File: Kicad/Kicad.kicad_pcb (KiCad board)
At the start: 4 copper layers, 6 parts, among them J1 USB_C_Receptacle_USB2.0, U1 MIMXRT685SFVKB, X1 ECS-2520MV-xxx-xx

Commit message: power section
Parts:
- D1: moved to F.Cu
- J1: footprint Connector_USB:USB_C_Receptacle_Amphenol_12401548E4-2A -> Connector_USB:USB_C_Receptacle_HRO_TYPE-C-31-M-12; moved to F.Cu
- moved X1 33.8 mm to (95.2, 66.3), turned to 0 degrees
- moved J1 12.4 mm to (76.5, 77.7), turned to -90 degrees
- moved L1 12.1 mm to (86.0, 82.0)
- moved U1 10.9 mm to (97.5, 74.5), turned to 180 degrees
- moved D1 10.4 mm to (86.2, 77.8), turned to -90 degrees
- moved C1 8.39 mm to (86.5, 85.0)
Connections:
- U1 pad A13: (no net) -> +1V8
- U1 pad B11: VDD1V8 -> +1V8
- U1 pad B16: (no net) -> /DSP/MODE1
- U1 pad C13: VDD_AO1V8 -> +1V8
- U1 pad C16: VDD1V8 -> +1V8
- U1 pad C17: VDD1V8 -> +1V8
- U1 pad D13: VDD_AO1V8 -> +1V8
- U1 pad E10: VDDIO_1 -> +3V3
- U1 pad E15: VDD1V8 -> +1V8
- U1 pad E4: unconnected-(U1-PadE4) -> +1V8
- U1 pad E6: VDDIO_1 -> +3V3
- U1 pad E8: VDDIO_1 -> +3V3
- U1 pad F13: VDD1V8 -> +1V8
- U1 pad F5: VDDIO_0 -> +3V3
- U1 pad G14: VDD1V8 -> +1V8
- U1 pad H13: VDDIO_1 -> +3V3
- U1 pad H14: VDDIO_1 -> +3V3
- U1 pad H5: VDDIO_0 -> +3V3
- U1 pad K13: VDDIO_1 -> +3V3
- U1 pad K5: VDDIO_0 -> +3V3
- U1 pad L14: VDDIO_1 -> +3V3
- U1 pad L4: VDD1V8 -> +1V8
- U1 pad M5: VDDIO_0 -> +3V3
- U1 pad N10: VDDIO_0 -> +3V3
- U1 pad N12: VDDIO_2 -> +3V3
- U1 pad N6: VDDIO_0 -> +3V3
- U1 pad N8: VDDIO_0 -> +3V3
- U1 pad P11: VDDIO_2 -> +3V3
- U1 pad P12: VDDIO_2 -> +3V3
- U1 pad R15: VDD1V8 -> +1V8
- U1 pad R17: /DSP/USB1_DP -> /USB/D+
- U1 pad T17: /DSP/USB1_DM -> /USB/D-
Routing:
- net GND: track 2.06 -> 0.00 mm, vias 3 -> 0
- net /DSP/XTALOUT: track 1.31 -> 0.00 mm
- net VDDIO_1: track 1.00 -> 0.00 mm, vias 2 -> 0
- net VDDIO_0: track 1.00 -> 0.00 mm, vias 2 -> 0
- net VDDIO_2: track 0.50 -> 0.00 mm, vias 1 -> 0
- net VDDCORE: track 0.50 -> 0.00 mm, vias 1 -> 0
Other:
- copper layers 4 -> 2

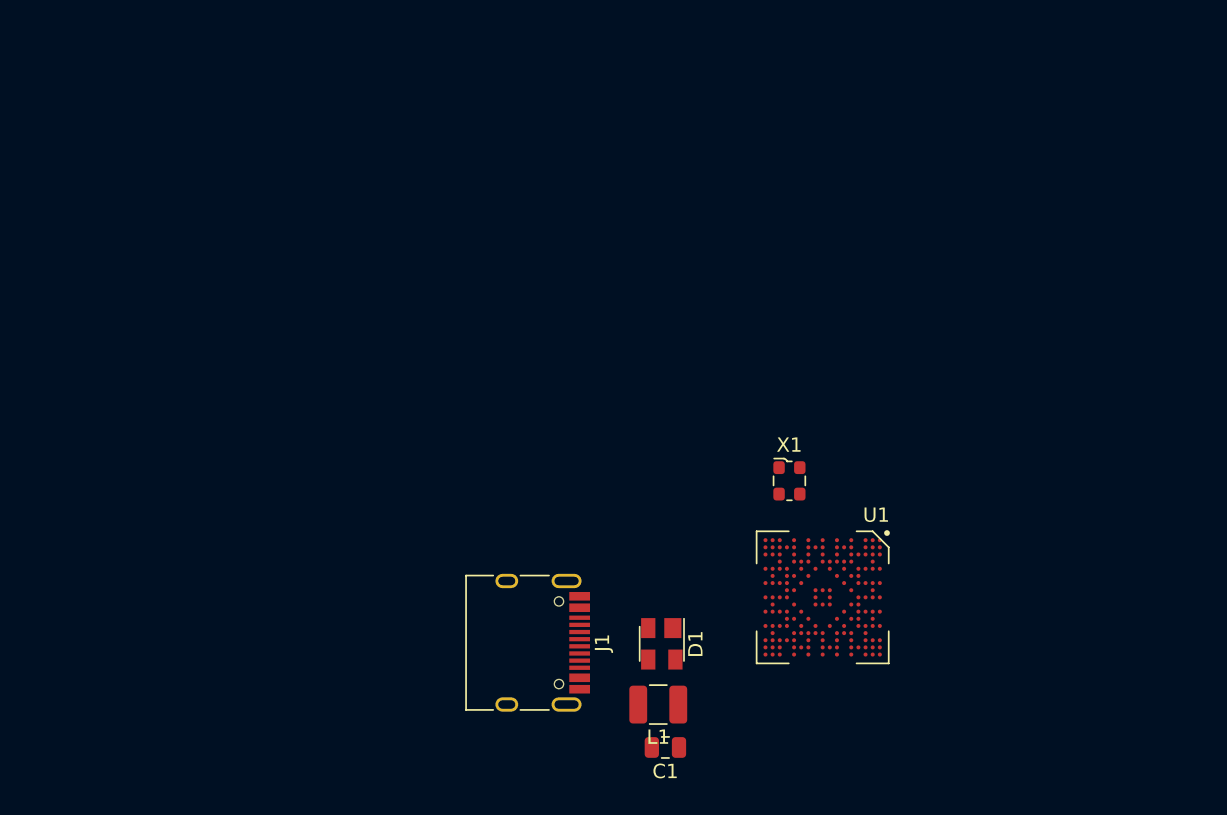
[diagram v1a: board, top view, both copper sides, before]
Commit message: Basic Power layout done
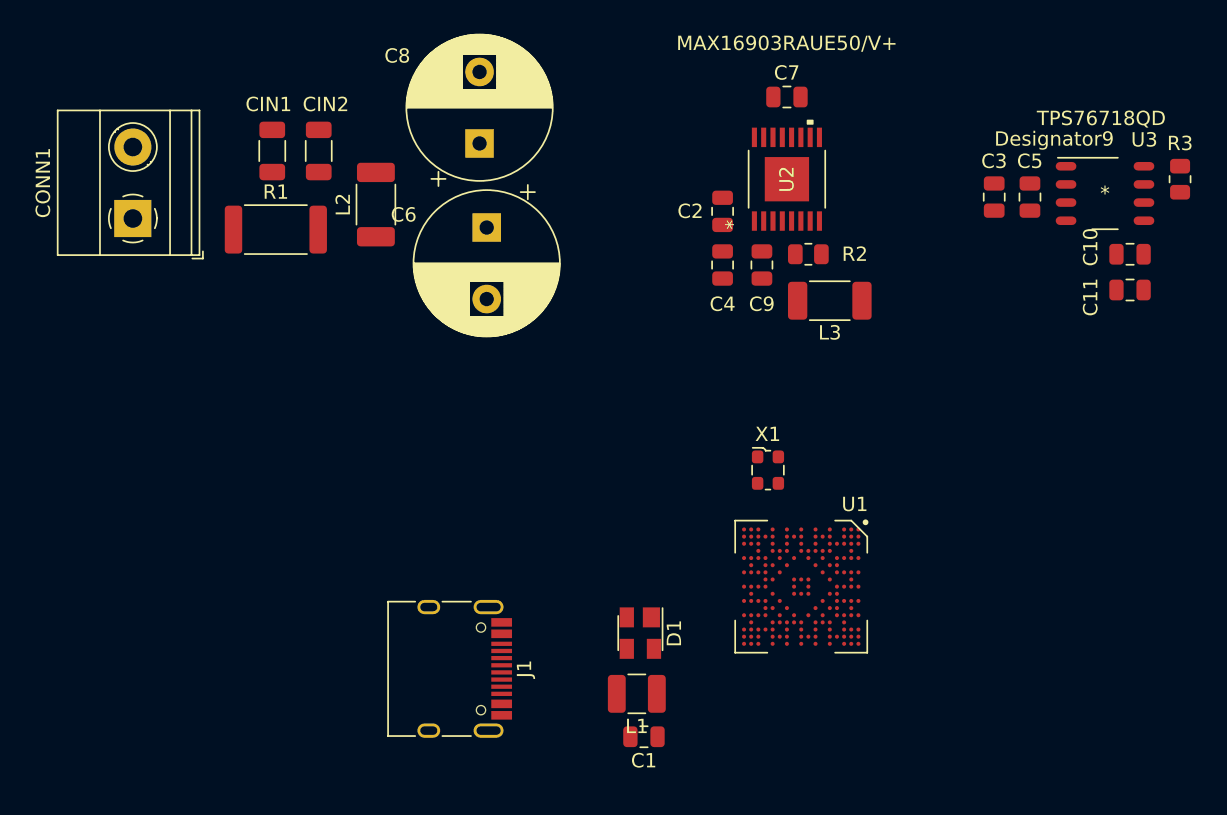
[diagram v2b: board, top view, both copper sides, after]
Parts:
- added C10: 10uF, Capacitor_SMD:C_0805_2012Metric, F.Cu at (119.0, 50.5)
- added C11: 10uF, Capacitor_SMD:C_0805_2012Metric, F.Cu at (119.0, 53.0)
- added C2: 4u7, Capacitor_SMD:C_0805_2012Metric, F.Cu at (90.5, 47.5)
- added C3: 1u, Capacitor_SMD:C_0805_2012Metric, F.Cu at (109.5, 46.5)
- added C4: 4u7, Capacitor_SMD:C_0805_2012Metric, F.Cu at (90.5, 51.2)
- added C5: 1u, Capacitor_SMD:C_0805_2012Metric, F.Cu at (112.0, 46.5)
- added C6: 100uF, Capacitor_THT:CP_Radial_D10.0mm_P5.00mm, F.Cu at (74.0, 48.6)
- added C7: 1u, Capacitor_SMD:C_0805_2012Metric, F.Cu at (95.0, 39.5)
- added C8: 100uF, Capacitor_THT:CP_Radial_D10.0mm_P5.00mm, F.Cu at (73.5, 42.8)
- added C9: 1u, Capacitor_SMD:C_0805_2012Metric, F.Cu at (93.2, 51.2)
- added CIN1: 0.022uF, Capacitor_SMD:C_1206_3216Metric, F.Cu at (59.0, 43.3)
- added CIN2: 0.022uF, Capacitor_SMD:C_1206_3216Metric, F.Cu at (62.2, 43.3)
- added CONN1: Screw_Terminal_01x02, TerminalBlock_Phoenix:TerminalBlock_Phoenix_MKDS-1,5-2_1x02_P5.00mm_Horizontal, F.Cu at (49.2, 48.0)
- added L2: 47, Inductor_SMD:L_2010_5025Metric, F.Cu at (66.2, 47.0)
- added L3: 4u7, Inductor_SMD:L_2010_5025Metric, F.Cu at (98.0, 53.8)
- added R1: 0.1R, Resistor_SMD:R_2512_6332Metric, F.Cu at (59.2, 48.8)
- added R2: 20k, Resistor_SMD:R_0805_2012Metric, F.Cu at (96.5, 50.5)
- added R3: 10k, Resistor_SMD:R_0805_2012Metric, F.Cu at (122.5, 45.2)
- added U2: MAX16903RAUE50/V+, project_footprints:MAX16903RAUE50&slash_V&plus_, F.Cu at (95.0, 45.2)
- added U3: TPS76718QD, project_footprints:TPS76718QD, F.Cu at (117.2, 46.2)
- moved J1 5.75 mm to (71.0, 79.5)
- moved C1 1.68 mm to (85.0, 84.2)
- moved D1 1.68 mm to (84.8, 77.0)
- moved L1 1.68 mm to (84.5, 81.2)
- moved U1 1.68 mm to (96.0, 73.8)
- moved X1 1.68 mm to (93.7, 65.6)

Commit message: working on DSP
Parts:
- added C12: 0.1u, Capacitor_SMD:C_0805_2012Metric, F.Cu at (141.8, 101.7)
- added C13: 1u, Capacitor_SMD:C_0805_2012Metric, F.Cu at (152.0, 95.2)
- added C14: 10u, Capacitor_SMD:C_0805_2012Metric, F.Cu at (154.2, 98.2)
- added C15: 0.1u, Capacitor_SMD:C_0805_2012Metric, F.Cu at (147.8, 104.2)
- added C16: 2.2u, Capacitor_SMD:C_0805_2012Metric, F.Cu at (153.0, 103.0)
- added C17: 0.1u, Capacitor_SMD:C_0805_2012Metric, F.Cu at (152.0, 98.2)
- added C18: 0.1u, Capacitor_SMD:C_0805_2012Metric, F.Cu at (140.2, 104.2)
- added C19: 0.1u, Capacitor_SMD:C_0805_2012Metric, F.Cu at (144.2, 104.2)
- added C20: 2.2u, Capacitor_SMD:C_0805_2012Metric, F.Cu at (147.8, 106.5)
- added C21: 10u, Capacitor_SMD:C_0805_2012Metric, F.Cu at (144.2, 106.5)
- added C22: C_Small, Capacitor_SMD:C_0805_2012Metric, F.Cu at (150.8, 104.5)
- added C23: 1000p, Capacitor_SMD:C_0805_2012Metric, F.Cu at (162.8, 104.0)
- added C24: 1000p, Capacitor_SMD:C_0805_2012Metric, F.Cu at (162.8, 97.5)
- added R10: 402, Resistor_SMD:R_0805_2012Metric, F.Cu at (165.8, 102.7)
- added R11: 402, Resistor_SMD:R_0805_2012Metric, F.Cu at (165.8, 98.7)
- added R12: 402, Resistor_SMD:R_0805_2012Metric, F.Cu at (165.8, 96.2)
- added R5: 402, Resistor_SMD:R_0805_2012Metric, F.Cu at (159.5, 105.2)
- added R6: 402, Resistor_SMD:R_0805_2012Metric, F.Cu at (159.5, 102.7)
- added R7: 402, Resistor_SMD:R_0805_2012Metric, F.Cu at (159.5, 98.7)
- added R8: 402, Resistor_SMD:R_0805_2012Metric, F.Cu at (159.5, 96.2)
- added R9: 402, Resistor_SMD:R_0805_2012Metric, F.Cu at (165.8, 105.2)
- added U4: PCM5242RHBR, project_footprints:PCM5242RHBR, F.Cu at (147.0, 99.2)
- C10: value 10uF -> 100uF; footprint Capacitor_SMD:C_0805_2012Metric -> Capacitor_THT:CP_Radial_D10.0mm_P5.00mm
- C11: value 10uF -> 1u
- C2: value 4u7 -> 1u
- C4: value 4u7 -> 10uF
- C5: value 1u -> 10uF
- C6: value 100uF -> 4u7; footprint Capacitor_THT:CP_Radial_D10.0mm_P5.00mm -> Capacitor_SMD:C_0805_2012Metric
- C7: value 1u -> 4u7
- R1: value 0.1R -> 10k; footprint Resistor_SMD:R_2512_6332Metric -> Resistor_SMD:R_0805_2012Metric
- R2: value 20k -> 0.1R; footprint Resistor_SMD:R_0805_2012Metric -> Resistor_SMD:R_2512_6332Metric
- R3: value 10k -> 20k
- U1: value MIMXRT685SFVKB -> VFBGA176_SOT1850-1_NXP; footprint project_footprints:BGA-289_17x17_9.0x9.0mm_v2 -> project_footprints:MIMXRT685SFVKB
- U2: value MAX16903RAUE50/V+ -> TPS76718QD; footprint project_footprints:MAX16903RAUE50&slash_V&plus_ -> project_footprints:TPS76718QD
- U3: value TPS76718QD -> MAX16903RAUE50/V+; footprint project_footprints:TPS76718QD -> project_footprints:MAX16903RAUE50&slash_V&plus_
- moved CONN1 127.5 mm to (175.9, 62.0), turned to -90 degrees
- moved CIN1 109.9 mm to (164.6, 73.5), turned to 0 degrees
- moved CIN2 100.7 mm to (160.1, 66.8), turned to 0 degrees
- moved L2 100.4 mm to (163.9, 70.5), turned to 180 degrees
- moved C8 87.9 mm to (160.0, 58.5), turned to 180 degrees
- moved C6 76.1 mm to (147.9, 66.8)
- moved R2 70.2 mm to (165.4, 64.2), turned to -90 degrees
- moved C7 57.5 mm to (145.6, 66.8), turned to -90 degrees
- moved R1 56.8 mm to (114.3, 62.6), turned to 180 degrees
- moved X1 52.9 mm to (125.8, 107.7)
- moved L3 48.7 mm to (146.4, 59.0), turned to 90 degrees
- moved C10 45.4 mm to (157.8, 74.2)
- moved C9 43.4 mm to (134.9, 63.5)
- moved C2 39.7 mm to (128.1, 60.3), turned to -90 degrees
- moved U1 39.7 mm to (127.8, 97.5)
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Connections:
- C10 pad 1: /POWER/VDD_1V8 -> Net-(C10-Pad1)
- C11 pad 1: /POWER/VDD_1V8 -> /externl_circuits/BST
- C11 pad 2: GND -> /externl_circuits/Buck_LX
- C2 pad 1: /POWER/VSUP -> /POWER/IN
- C4 pad 1: /POWER/VSUP -> /POWER/VDD_1V8
- C5 pad 1: /POWER/IN -> /POWER/VDD_1V8
- C6 pad 1: Net-(C6-Pad1) -> /externl_circuits/VSUP
- C7 pad 1: /POWER/BIAS -> /externl_circuits/VSUP
- C8 pad 1: Net-(C6-Pad1) -> Net-(C10-Pad1)
- C9 pad 1: /POWER/BST -> /externl_circuits/BIAS
- C9 pad 2: /POWER/LX -> GND
- CIN2 pad 2: Net-(C6-Pad1) -> Net-(C10-Pad1)
- CONN1 pad 1: /POWER/VSUP -> /externl_circuits/VSUP
- L2 pad 2: Net-(C6-Pad1) -> Net-(C10-Pad1)
- L3 pad 1: /POWER/LX -> /externl_circuits/Buck_LX
- L3 pad 2: /POWER/5V_BUCK -> /externl_circuits/5V_BUCK
- R1 pad 1: /POWER/VSUP -> /POWER/~{RESET}
- R1 pad 2: Net-(CIN1-Pad2) -> /POWER/VDD_1V8
- R2 pad 1: /POWER/LX -> /externl_circuits/VSUP
- R2 pad 2: /POWER/PGOOD -> Net-(CIN1-Pad2)
- R3 pad 1: /POWER/~{RESET} -> /externl_circuits/Buck_LX
- R3 pad 2: /POWER/VDD_1V8 -> /externl_circuits/PGOOD
- U2 pad 1: /POWER/BST -> GND
- U2 pad 2: /POWER/VSUP -> GND
- U2 pad 3: /POWER/VSUP -> /POWER/IN
- U2 pad 4: /POWER/LX -> /POWER/IN
- U2 pad 5: /POWER/LX -> /POWER/VDD_1V8
- U2 pad 6: GND -> /POWER/VDD_1V8
- U2 pad 7: GND -> unconnected-(U2-Pad7)
- U2 pad 8: /POWER/5V_BUCK -> /POWER/~{RESET}
- U3 pad 1: GND -> /externl_circuits/BST
- U3 pad 2: GND -> /externl_circuits/VSUP
- U3 pad 3: /POWER/IN -> /externl_circuits/VSUP
- U3 pad 4: /POWER/IN -> /externl_circuits/Buck_LX
- U3 pad 5: /POWER/VDD_1V8 -> /externl_circuits/Buck_LX
- U3 pad 6: /POWER/VDD_1V8 -> GND
- U3 pad 7: unconnected-(U3-Pad7) -> GND
- U3 pad 8: /POWER/~{RESET} -> /externl_circuits/5V_BUCK
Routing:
- added copper zone on In1.Cu, net GND
- added copper zone on In2.Cu, net GND
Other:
- board outline added: 87.2 x 58.2 mm
- copper layers 2 -> 4

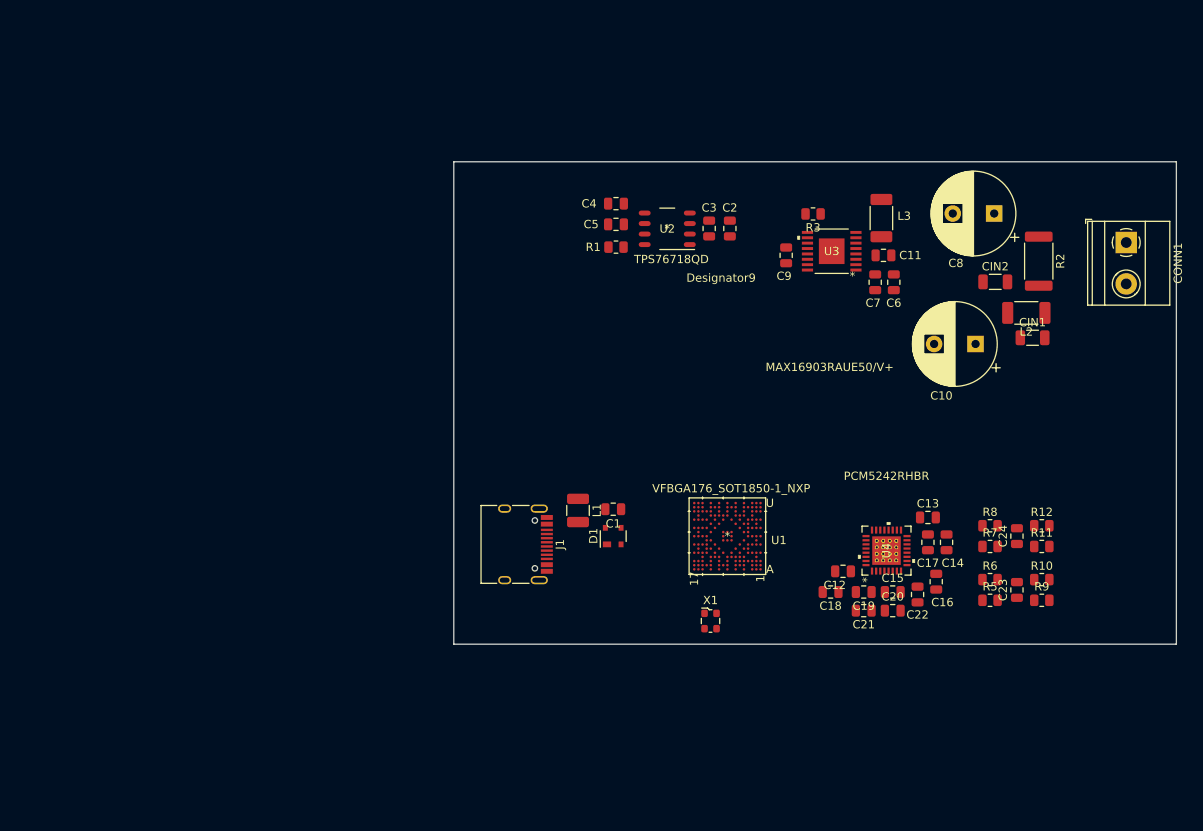
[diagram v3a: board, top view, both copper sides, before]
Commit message: updated footprints, basic pcb laypout
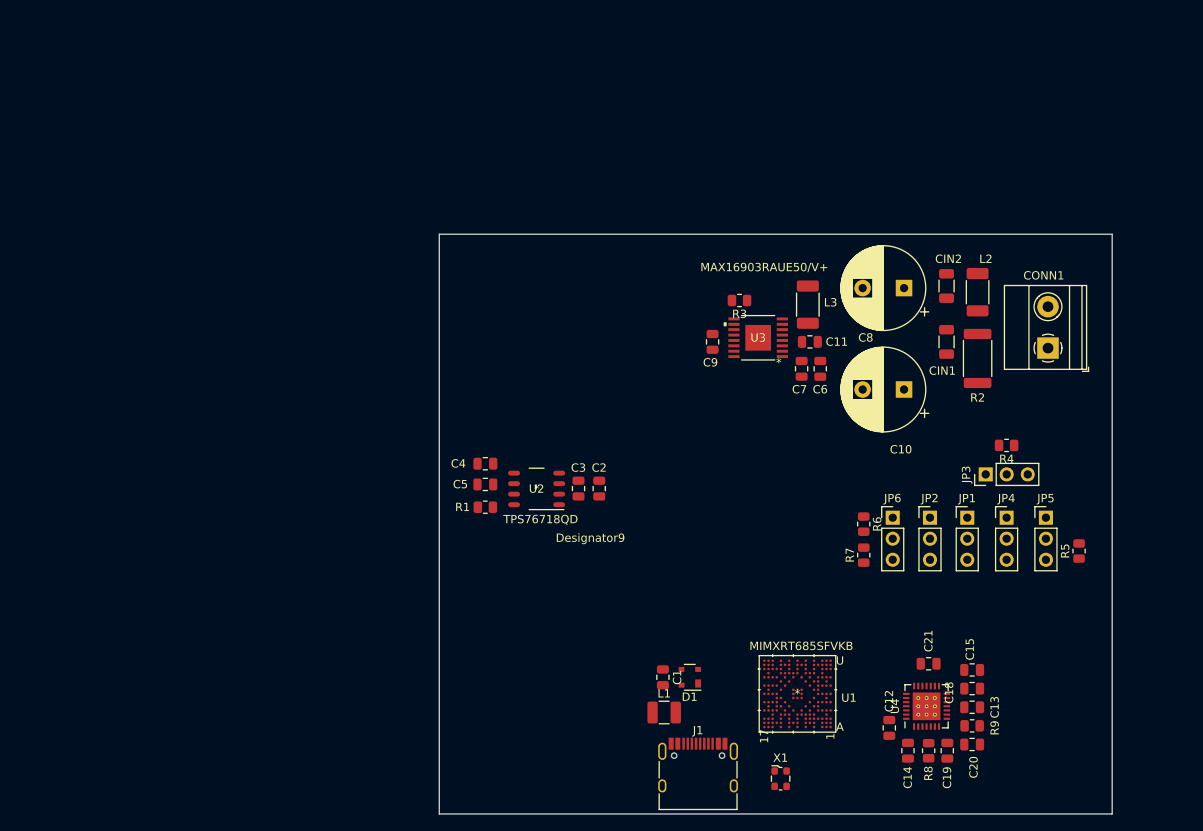
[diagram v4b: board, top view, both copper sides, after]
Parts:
- removed C16: 2.2u, Capacitor_SMD:C_0805_2012Metric
- removed C17: 0.1u, Capacitor_SMD:C_0805_2012Metric
- removed C22: C_Small, Capacitor_SMD:C_0805_2012Metric
- removed C23, C24: 1000p, Capacitor_SMD:C_0805_2012Metric
- removed R10, R11, R12: 402, Resistor_SMD:R_0805_2012Metric
- added JP1: Jumper_3_Open, Connector_PinHeader_2.54mm:PinHeader_1x03_P2.54mm_Vertical, F.Cu at (156.8, 95.2)
- added JP2: Jumper_3_Open, Connector_PinHeader_2.54mm:PinHeader_1x03_P2.54mm_Vertical, F.Cu at (152.2, 95.2)
- added JP3: Jumper_3_Open, Connector_PinHeader_2.54mm:PinHeader_1x03_P2.54mm_Vertical, F.Cu at (159.0, 90.0)
- added JP4: Jumper_3_Open, Connector_PinHeader_2.54mm:PinHeader_1x03_P2.54mm_Vertical, F.Cu at (161.5, 95.2)
- added JP5: Jumper_3_Open, Connector_PinHeader_2.54mm:PinHeader_1x03_P2.54mm_Vertical, F.Cu at (166.2, 95.2)
- added JP6: Jumper_3_Open, Connector_PinHeader_2.54mm:PinHeader_1x03_P2.54mm_Vertical, F.Cu at (147.8, 95.2)
- added R4: 47k, Resistor_SMD:R_0805_2012Metric, F.Cu at (161.5, 86.5)
- C12, C18: value 0.1u -> 1u
- C14, C21: value 10u -> 1u
- C15: value 0.1u -> 4u7
- C19: value 0.1u -> 2n2
- C20: value 2.2u -> 2n2
- R5, R6, R7: value 402 -> 47k
- R8, R9: value 402 -> 300
- U1: value VFBGA176_SOT1850-1_NXP -> MIMXRT685SFVKB
- U4: value PCM5242RHBR -> ES9033; footprint project_footprints:PCM5242RHBR -> Package_DFN_QFN:QFN-28-1EP_5x5mm_P0.5mm_EP3.35x3.35mm_ThermalVias
- moved J1 35.9 mm to (124.2, 126.6), turned to 0 degrees
- moved U2 35.1 mm to (104.8, 91.8)
- moved C2 35.1 mm to (112.3, 91.7)
- moved C3 35.1 mm to (109.8, 91.7)
- moved C4 35.1 mm to (98.6, 88.7)
- moved C5 35.1 mm to (98.6, 91.2)
- moved R1 35.1 mm to (98.6, 94.0)
- moved R8 28.2 mm to (152.1, 123.4), turned to -90 degrees
- moved L1 26.5 mm to (120.2, 118.8), turned to 0 degrees
- moved C14 25.6 mm to (149.6, 123.4), turned to -90 degrees
- moved C13 23.5 mm to (157.3, 118.1)
- moved C19 21.7 mm to (154.3, 123.4), turned to -90 degrees
- moved C1 21.2 mm to (120.0, 114.5), turned to 90 degrees
- moved X1 20.8 mm to (134.2, 126.7)
- moved U1 20.8 mm to (136.2, 116.5)
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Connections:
- net /DAC/DIN_DAC renamed Net-(C16-Pad1)
- net /DAC/SCK_DAC renamed /DAC/DAC_MCLK
- C12 pad 1: /DAC/DAC_MUTE -> +3.3V
- C13 pad 1: /DAC/DAC_VCOM -> +3.3V
- C14 pad 1: +3V3 -> +3.3V
- C15 pad 1: +3V3 -> /DAC/PGND
- C18 pad 1: +1V8 -> Net-(C18-Pad1)
- C19 pad 1: +1V8 -> GND
- C19 pad 2: Net-(C19-Pad2) -> /DAC/DAC_OUT1
- C20 pad 1: +3V3 -> GND
- C20 pad 2: GND -> /DAC/DAC_OUT2
- C21 pad 1: +1V8 -> +3.3V
- R5 pad 1: /DAC/DAC_OUTLP -> Net-(JP5-Pad3)
- R5 pad 2: Net-(C23-Pad1) -> GND
- R6 pad 1: /DAC/DAC_OUTLN -> Net-(JP6-Pad1)
- R6 pad 2: Net-(C23-Pad2) -> +3.3V
- R7 pad 1: /DAC/DAC_OUTRN -> Net-(JP6-Pad3)
- R7 pad 2: Net-(C24-Pad1) -> GND
- R8 pad 1: /DAC/DAC_OUTRP -> Net-(R8-Pad1)
- R8 pad 2: Net-(C24-Pad2) -> /DAC/DAC_OUT1
- R9 pad 1: Net-(C23-Pad1) -> Net-(R9-Pad1)
- R9 pad 2: /DAC/OUTRP -> /DAC/DAC_OUT2
- U4 pad 1: /DAC/DAC_MUTE -> +3.3V
- U4 pad 10: /DAC/DAC_OUTLP -> unconnected-(U4-Pad10)
- U4 pad 11: /DAC/DAC_OUTLN -> GND
- U4 pad 12: /DAC/DAC_OUTRN -> Net-(C18-Pad1)
- U4 pad 13: /DAC/DAC_OUTRP -> GND
- U4 pad 14: +3V3 -> /DAC/PGND
- U4 pad 15: GND -> Net-(C17-Pad1)
- U4 pad 16: /DAC/DAC_VCOM -> Net-(C17-Pad2)
- U4 pad 17: /DAC/SDA_DAC -> +3.3V
- U4 pad 18: /DAC/SCL_DAC -> GND
- U4 pad 19: unconnected-(U4-Pad19) -> /DAC/HW2
- U4 pad 2: Net-(C19-Pad2) -> /DAC/DAC_ENABLE
- U4 pad 20: unconnected-(U4-Pad20) -> /DAC/MUTE_CTRL
- U4 pad 21: unconnected-(U4-Pad21) -> /DAC/HW1
- U4 pad 22: unconnected-(U4-Pad22) -> /DAC/HW0
- U4 pad 23: unconnected-(U4-Pad23) -> /DAC/DAC_SDO
- U4 pad 24: unconnected-(U4-Pad24) -> /DAC/DAC_WS
- U4 pad 25: unconnected-(U4-Pad25) -> /DAC/DAC_BCK
- U4 pad 27: /DAC/BCK_DAC -> GND
- U4 pad 29: unconnected-(U4-Pad29) -> GND
- U4 pad 3: GND -> /DAC/MODE
- U4 pad 4: +3V3 -> +3.3V
- U4 pad 5: +1V8 -> GND
- U4 pad 6: /DAC/DAC_CAP -> Net-(R8-Pad1)
- U4 pad 8: Net-(C22-Pad2) -> Net-(R9-Pad1)
- U4 pad 9: Net-(C16-Pad1) (its old number) -> +3.3V
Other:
- board size 87.2 x 58.2 mm -> 81.2 x 70 mm
